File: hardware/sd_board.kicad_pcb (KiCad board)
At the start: 2 copper layers, 39.4 x 27.9 mm, 13 parts, among them J1 Screw_Terminal_01x03, SW1 SW_SPST, SW2 SW_SPST, U1 PIC16F18346-SS_0, U2 VL53L1CXV0FY1

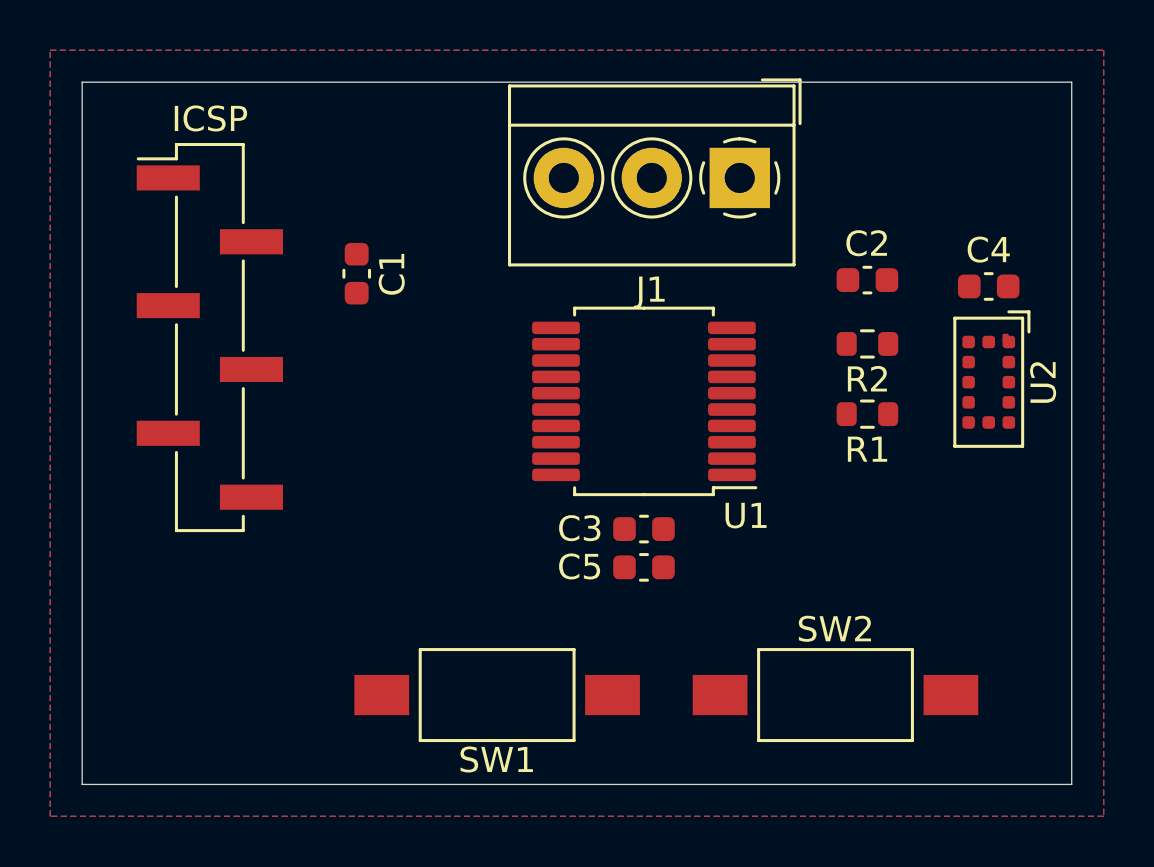
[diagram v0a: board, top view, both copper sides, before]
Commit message: add msp430 stuff to hardware. using terrible lib from snapeda, need to fix
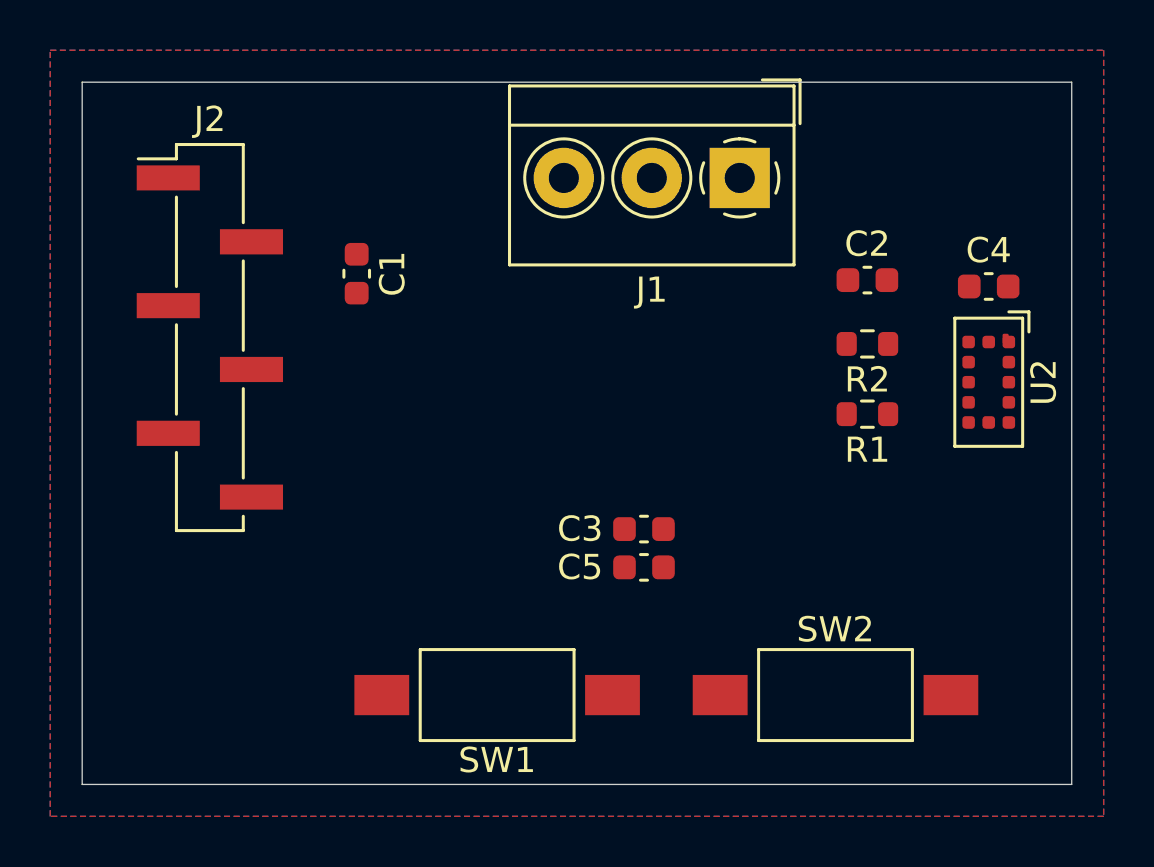
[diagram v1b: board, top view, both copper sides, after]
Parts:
- removed U1: PIC16F18346-SS_0, Package_SO:SSOP-20_5.3x7.2mm_P0.65mm
- renumbered ICSP to J2
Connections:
- J1 pad 2: Net-(J1-Pad2) -> (no net)
- J1 pad 3: Net-(J1-Pad3) -> (no net)
- J2 pad 1: Net-(J2-Pad1) -> (no net)
- J2 pad 4: Net-(J2-Pad4) -> (no net)
- J2 pad 5: Net-(J2-Pad5) -> (no net)
- SW1 pad 1: Net-(SW1-Pad1) -> (no net)
- SW2 pad 1: Net-(SW2-Pad1) -> (no net)
- U2 pad 5: XSHUT -> (no net)
- U2 pad 7: INT -> (no net)

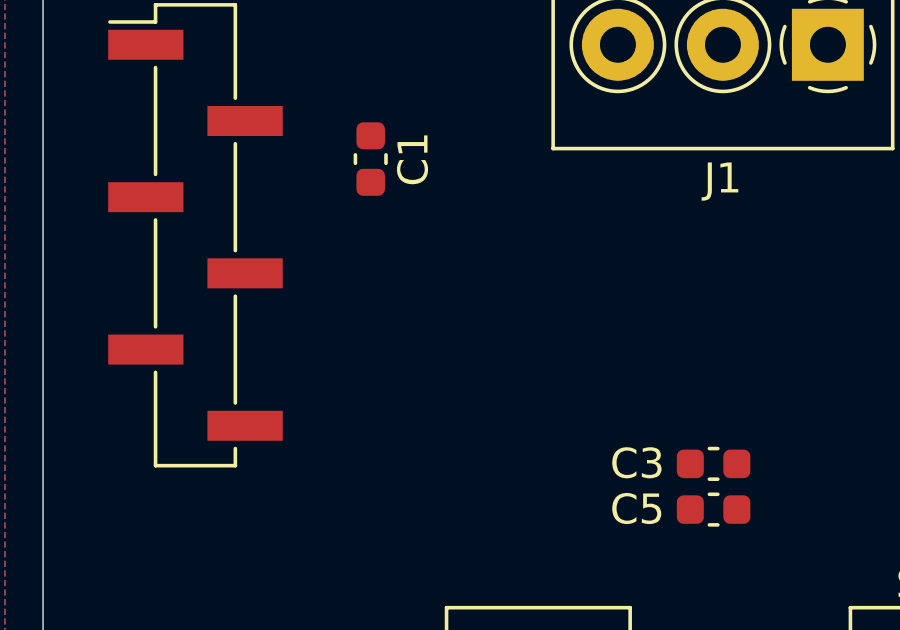
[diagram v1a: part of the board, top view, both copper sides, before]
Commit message: start of ssd1306 driver.. HD44780 displays are pigs
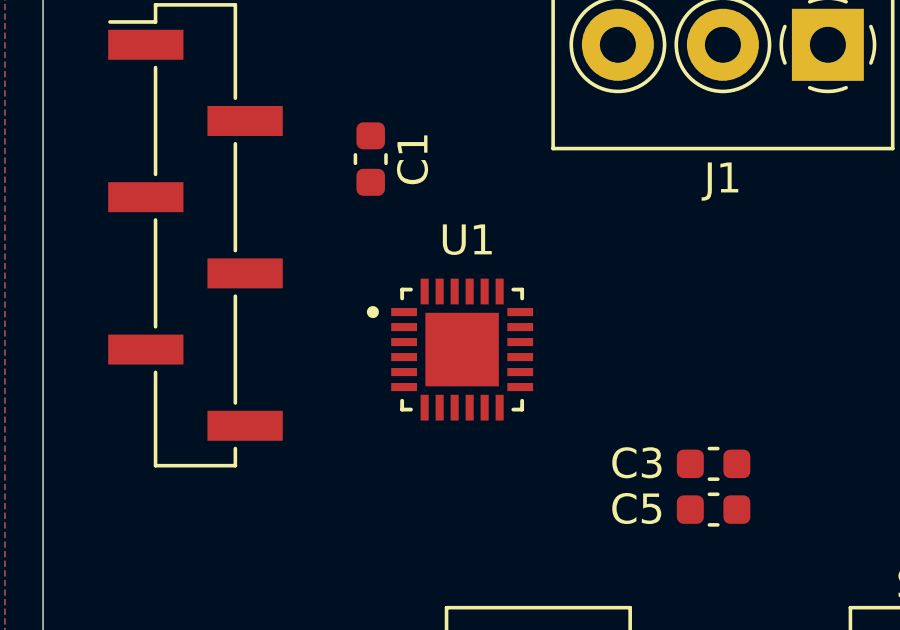
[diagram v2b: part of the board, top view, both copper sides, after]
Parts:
- added U1: MSP430FR2433IRGER, libraries:QFN50P400X400X100-25N, F.Cu at (128.3, 77.5)
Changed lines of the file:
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@@
     (tracks 0)
     (zones 0)
-    (modules 12)
+    (modules 13)
     (nets 5)
   )
@@
     (add_net "Net-(SW1-Pad1)")
     (add_net "Net-(SW2-Pad1)")
+    (add_net "Net-(U1-Pad1)")
+    (add_net "Net-(U1-Pad10)")
+    (add_net "Net-(U1-Pad11)")
+    (add_net "Net-(U1-Pad12)")
+    (add_net "Net-(U1-Pad13)")
+    (add_net "Net-(U1-Pad14)")
+    (add_net "Net-(U1-Pad15)")
+    (add_net "Net-(U1-Pad16)")
+    (add_net "Net-(U1-Pad17)")
+    (add_net "Net-(U1-Pad18)")
+    (add_net "Net-(U1-Pad19)")
+    (add_net "Net-(U1-Pad2)")
+    (add_net "Net-(U1-Pad20)")
+    (add_net "Net-(U1-Pad21)")
+    (add_net "Net-(U1-Pad22)")
+    (add_net "Net-(U1-Pad23)")
+    (add_net "Net-(U1-Pad24)")
+    (add_net "Net-(U1-Pad3)")
+    (add_net "Net-(U1-Pad4)")
+    (add_net "Net-(U1-Pad5)")
+    (add_net "Net-(U1-Pad6)")
+    (add_net "Net-(U1-Pad7)")
+    (add_net "Net-(U1-Pad8)")
+    (add_net "Net-(U1-Pad9)")
     (add_net "Net-(U2-Pad8)")
     (add_net SCL)
@@
     (add_net XSHUT)
   )
+  (module libraries:QFN50P400X400X100-25N (layer F.Cu)
+    (at 128.27 77.47)
+    (fp_text reference U1 (at 0.175 -3.635) (layer F.SilkS)
+      (effects (font (size 1 1) (thickness 0.15)))
+    )
+    (fp_text value MSP430FR2433IRGER (at 10.335 3.635) (layer F.Fab)
+      (effects (font (size 1 1) (thickness 0.15)))
+    )
+    (fp_line (start 2.615 2.615) (end 2.615 -2.615) (layer F.CrtYd) (width 0.05))
+    (fp_line (start -2.615 2.615) (end -2.615 -2.615) (layer F.CrtYd) (width 0.05))
+    (fp_line (start -2.615 -2.615) (end 2.615 -2.615) (layer F.CrtYd) (width 0.05))
+    (fp_line (start -2.615 2.615) (end 2.615 2.615) (layer F.CrtYd) (width 0.05))
+    (fp_line (start -2 -2) (end -2 -1.705) (layer F.SilkS) (width 0.127))
+    (fp_line (start -2 2) (end -2 1.705) (layer F.SilkS) (width 0.127))
+    (fp_line (start 2 -2) (end 2 -1.705) (layer F.SilkS) (width 0.127))
+    (fp_line (start 2 2) (end 2 1.705) (layer F.SilkS) (width 0.127))
+    (fp_line (start -2 -2) (end -1.705 -2) (layer F.SilkS) (width 0.127))
+    (fp_line (start -2 2) (end -1.705 2) (layer F.SilkS) (width 0.127))
+    (fp_line (start 2 -2) (end 1.705 -2) (layer F.SilkS) (width 0.127))
+    (fp_line (start 2 2) (end 1.705 2) (layer F.SilkS) (width 0.127))
+    (fp_line (start -2 2) (end -2 -2) (layer F.Fab) (width 0.127))
+    (fp_line (start 2 2) (end 2 -2) (layer F.Fab) (width 0.127))
+    (fp_line (start 2 -2) (end -2 -2) (layer F.Fab) (width 0.127))
+    (fp_line (start 2 2) (end -2 2) (layer F.Fab) (width 0.127))
+    (fp_circle (center -2.975 -1.25) (end -2.875 -1.25) (layer F.Fab) (width 0.2))
+    (fp_circle (center -2.975 -1.25) (end -2.875 -1.25) (layer F.SilkS) (width 0.2))
+    (fp_poly (pts (xy -0.775 -0.775) (xy 0.775 -0.775) (xy 0.775 0.775) (xy -0.775 0.775)) (layer F.Paste) (width 0.01))
+    (pad 25 smd rect (at 0 0) (size 2.45 2.45) (layers F.Cu F.Mask))
+    (pad 18 smd rect (at 1.935 -1.25) (size 0.86 0.27) (layers F.Cu F.Paste F.Mask))
+    (pad 17 smd rect (at 1.935 -0.75) (size 0.86 0.27) (layers F.Cu F.Paste F.Mask))
+    (pad 16 smd rect (at 1.935 -0.25) (size 0.86 0.27) (layers F.Cu F.Paste F.Mask))
+    (pad 15 smd rect (at 1.935 0.25) (size 0.86 0.27) (layers F.Cu F.Paste F.Mask))
+    (pad 14 smd rect (at 1.935 0.75) (size 0.86 0.27) (layers F.Cu F.Paste F.Mask))
+    (pad 13 smd rect (at 1.935 1.25) (size 0.86 0.27) (layers F.Cu F.Paste F.Mask))
+    (pad 6 smd rect (at -1.935 1.25) (size 0.86 0.27) (layers F.Cu F.Paste F.Mask))
+    (pad 5 smd rect (at -1.935 0.75) (size 0.86 0.27) (layers F.Cu F.Paste F.Mask))
+    (pad 4 smd rect (at -1.935 0.25) (size 0.86 0.27) (layers F.Cu F.Paste F.Mask))
+    (pad 3 smd rect (at -1.935 -0.25) (size 0.86 0.27) (layers F.Cu F.Paste F.Mask))
+    (pad 2 smd rect (at -1.935 -0.75) (size 0.86 0.27) (layers F.Cu F.Paste F.Mask))
+    (pad 1 smd rect (at -1.935 -1.25) (size 0.86 0.27) (layers F.Cu F.Paste F.Mask))
+    (pad 24 smd rect (at -1.25 -1.935) (size 0.27 0.86) (layers F.Cu F.Paste F.Mask))
+    (pad 23 smd rect (at -0.75 -1.935) (size 0.27 0.86) (layers F.Cu F.Paste F.Mask))
+    (pad 22 smd rect (at -0.25 -1.935) (size 0.27 0.86) (layers F.Cu F.Paste F.Mask))
+    (pad 21 smd rect (at 0.25 -1.935) (size 0.27 0.86) (layers F.Cu F.Paste F.Mask))
+    (pad 20 smd rect (at 0.75 -1.935) (size 0.27 0.86) (layers F.Cu F.Paste F.Mask))
+    (pad 19 smd rect (at 1.25 -1.935) (size 0.27 0.86) (layers F.Cu F.Paste F.Mask))
+    (pad 12 smd rect (at 1.25 1.935) (size 0.27 0.86) (layers F.Cu F.Paste F.Mask))
+    (pad 11 smd rect (at 0.75 1.935) (size 0.27 0.86) (layers F.Cu F.Paste F.Mask))
+    (pad 10 smd rect (at 0.25 1.935) (size 0.27 0.86) (layers F.Cu F.Paste F.Mask))
+    (pad 9 smd rect (at -0.25 1.935) (size 0.27 0.86) (layers F.Cu F.Paste F.Mask))
+    (pad 8 smd rect (at -0.75 1.935) (size 0.27 0.86) (layers F.Cu F.Paste F.Mask))
+    (pad 7 smd rect (at -1.25 1.935) (size 0.27 0.86) (layers F.Cu F.Paste F.Mask))
+    (model ${KIPRJMOD}/libraries/MSP430FR2433IRGER.step
+      (at (xyz 0 0 0))
+      (scale (xyz 1 1 1))
+      (rotate (xyz -90 0 0))
+    )
+  )
   (module Connector_PinHeader_2.54mm:PinHeader_1x06_P2.54mm_Vertical_SMD_Pin1Left (layer F.Cu)
